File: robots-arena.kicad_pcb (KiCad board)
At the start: 2 copper layers, 86.4 x 54.6 mm, 48 parts, among them J1 SMA, P1 CONN_01X03, P10 CONN_01X03, P11 CONN_01X04, P12 CONN_01X05, P13 CONN_01X04, P2 CONN_01X03, P3 CONN_01X03, P4 CONN_01X03, P5 CONN_01X03, P6 CONN_01X03, P7 CONN_01X03, P8 CONN_23X2, P9 CONN_23X2, SW1 DIPS_02, U1 MPU-9150, U2 FGPMMOPA6H, U3 LPS331AP, U4 CAT24C256W

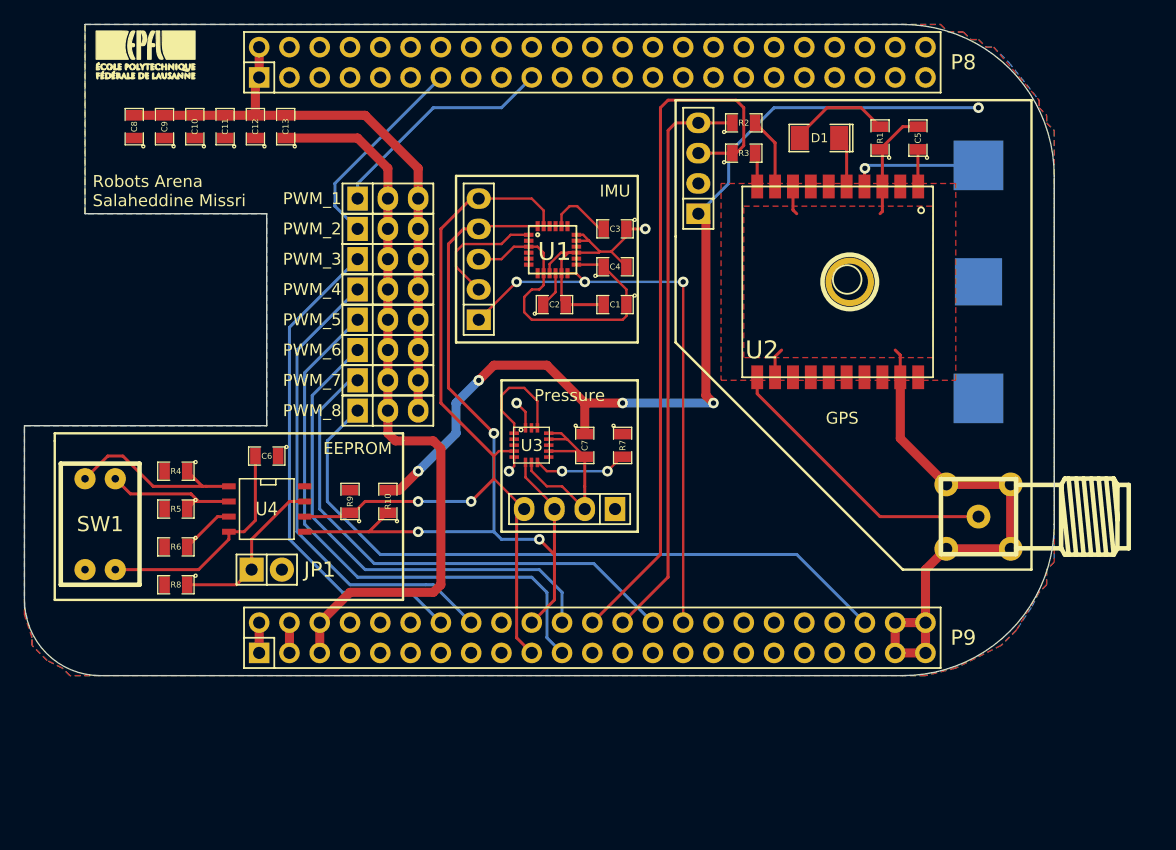
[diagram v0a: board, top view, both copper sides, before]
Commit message: .sch done, .net done, components on PCB done
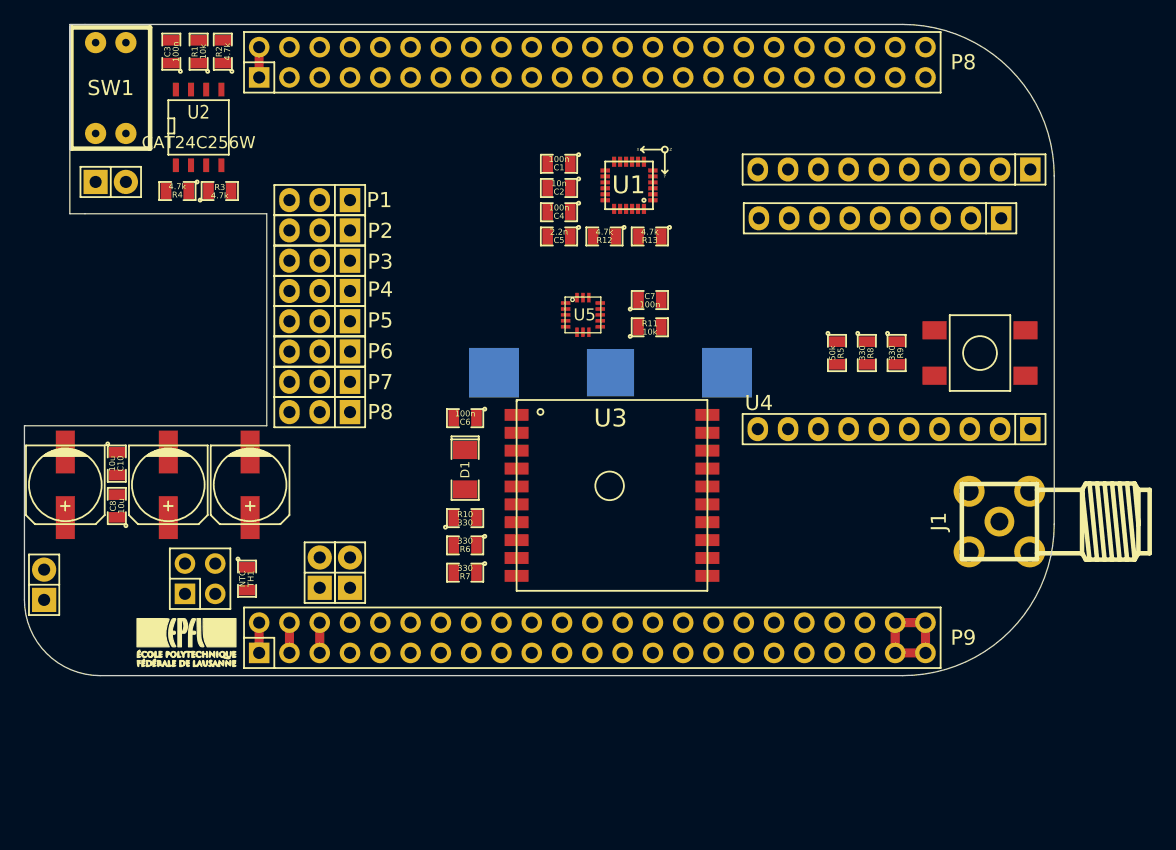
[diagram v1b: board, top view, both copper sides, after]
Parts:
- removed 1PIN: P***, Connect:1pin
- removed C13: 470u, SMD_Packages:SMD-0805
- removed the G*** at (172.7, 108.6)
- removed P10: CONN_01X03, Pin_Headers:Pin_Header_Straight_1x03
- added JP2: JUMPER, Pin_Headers:Pin_Header_Straight_1x02, F.Cu at (127.0, 113.3)
- added JP3: JUMPER, Pin_Headers:Pin_Header_Straight_1x02, F.Cu at (129.5, 113.3)
- added P8: CONN_PWM, Pin_Headers:Pin_Header_Straight_1x03, F.Cu at (127.0, 99.8)
- added R11: 10k, SMD_Packages:SMD-0805, F.Cu at (154.7, 92.7)
- added R12: 4.7k, SMD_Packages:SMD-0805, F.Cu at (150.9, 85.1)
- added R13: 4.7k, SMD_Packages:SMD-0805, F.Cu at (154.7, 85.1)
- added SW2: SW_PUSH, RA_connectors:SW_PUSH_SMD, F.Cu at (182.4, 94.2)
- added TH1: NTC, SMD_Packages:SMD-0805, F.Cu at (120.9, 113.8)
- added U5: LPS331AP, RA_sensors:LPS331AP, F.Cu at (147.6, 90.2)
- BT1: footprint RobotsArena:BK-885 -> RA_connectors:BK-885
- C1: value 10n -> 100n
- C11, C12, C9: value 10u -> 470u; footprint SMD_Packages:SMD-0805 -> Capacitors_SMD:c_elec_6.3x7.7
- C2: value 100n -> 10n
- C3: value 2.2n -> 100n
- C5: value 100n -> 2.2n
- J1: footprint RobotsArena:SMA -> RA_connectors:SMA-CONN
- P1, P2, P3, P4, P5, P6, P7: value CONN_01X03 -> CONN_PWM
- P11: value CONN_01X04 -> CONN_01X09; footprint Pin_Headers:Pin_Header_Straight_1x04 -> Pin_Headers:Pin_Header_Straight_1x09
- P12: value CONN_01X05 -> CONN_02X02; footprint Pin_Headers:Pin_Header_Straight_1x05 -> Pin_Headers:Pin_Header_Straight_2x02
- P13: value CONN_01X04 -> JST_2; footprint Pin_Headers:Pin_Header_Straight_1x04 -> Pin_Headers:Pin_Header_Straight_1x02
- R1: value 330 -> 10k
- R10, R6, R9: value 4.7k -> 330
- R2, R3: value 330 -> 4.7k
- R5: value 4.7k -> 50k
- R7, R8: value 10k -> 330
- SW1: value DIPS_02 -> DIPSW_02; footprint RobotsArena:DIPS-DS02 -> RA_connectors:DIPS-DS02
- U1: footprint RobotsArena:MPU-9150 -> RA_sensors:MPU-9150
- U2: value FGPMMOPA6H -> CAT24C256W; footprint RobotsArena:10011-FGPMMOPA6H -> SMD_Packages:SOIC-8-N
- U3: value LPS331AP -> MTK339; footprint RobotsArena:LPS331AP -> RA_sensors:FGPMMOPA6H
- U4: value CAT24C256W -> XBee_Header; footprint SMD_Packages:SOIC-8-N -> RA_connectors:XBEE-HEADER
- moved U2 61.8 mm to (116.8, 75.9), turned to 0 degrees
- moved R8 61.1 mm to (172.9, 94.9), turned to 270 degrees
- moved U4 57.9 mm to (177.8, 90.7)
- moved R1 57.6 mm to (116.8, 69.6)
- moved R5 57.0 mm to (170.4, 94.9), turned to 270 degrees
- moved G*** 49.4 mm to (115.8, 119.1)
- moved R9 47.5 mm to (175.4, 94.9), turned to 270 degrees
- moved P13 44.5 mm to (103.9, 114.3), turned to 90 degrees
- moved R2 44.1 mm to (118.9, 69.6), turned to 90 degrees
- moved R3 44.1 mm to (118.6, 81.3)
- moved D1 40.7 mm to (139.2, 104.6), turned to 270 degrees
- moved C3 40.1 mm to (114.6, 69.6), turned to 90 degrees
- moved SW1 36.6 mm to (109.5, 72.6)
- moved P12 35.6 mm to (117.0, 113.8), turned to 0 degrees
- moved JP1 35.0 mm to (109.5, 80.5)
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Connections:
- C10 pad 1: 3V3 -> +5V
- C11 pad 1: 3V3 -> +5V
- C12 pad 1: 3V3 -> +5V
- C2 pad 1: Net-(C2-Pad1) -> 3V3
- C3 pad 1: DGND -> 3V3
- C3 pad 2: Net-(C3-Pad2) -> DGND
- C4 pad 1: 3V3 -> Net-(C4-Pad1)
- C5 pad 1: 3V3 -> Net-(C5-Pad1)
- P11 pad 1: 3V3 -> Net-(P11-Pad1)
- P11 pad 2: DGND -> Net-(P11-Pad2)
- P11 pad 3: UART_1_TX -> Net-(P11-Pad3)
- P11 pad 4: UART_1_RX -> Net-(P11-Pad4)
- P12 pad 1: INT_M -> SENSE
- P12 pad 2: DGND -> SENSE
- P12 pad 3: 3V3 -> BAT-
- P12 pad 4: I2C_2_SDA -> TS
- P13 pad 1: 3V3 -> BAT-
- P13 pad 2: DGND -> SENSE
- P8 pad 16: Net-(P8-Pad16) -> INT_M
- P8 pad 18: Net-(P8-Pad18) -> BEE_DTR
- P8 pad 31: Net-(P8-Pad31) -> UART_5_CTS
- P8 pad 32: Net-(P8-Pad32) -> UART_5_RTS
- P8 pad 37: Net-(P8-Pad37) -> UART_5_TX
- P8 pad 38: Net-(P8-Pad38) -> UART_5_RX
- P9 pad 30: INT_M -> Net-(P9-Pad30)
- P9 pad 5: +5V -> BBB_VDD_5V
- P9 pad 6: +5V -> BBB_VDD_5V
- P9 pad 7: Net-(P9-Pad7) -> BBB_SYS_5V
- P9 pad 8: Net-(P9-Pad8) -> BBB_SYS_5V
- R1 pad 1: DGND -> Net-(JP1-Pad1)
- R1 pad 2: Net-(D1-Pad2) -> 3V3
- R10 pad 1: I2C_2_SDA -> Net-(D1-Pad2)
- R10 pad 2: 3V3 -> DGND
- R2 pad 1: UART_1_RX -> Net-(R2-Pad1)
- R2 pad 2: Net-(R2-Pad2) -> 3V3
- R3 pad 1: UART_1_TX -> Net-(R3-Pad1)
- R3 pad 2: Net-(R3-Pad2) -> 3V3
- R5 pad 1: Net-(R5-Pad1) -> 3V3
- R5 pad 2: 3V3 -> Net-(R5-Pad2)
- R6 pad 2: 3V3 -> UART_1_RX
- R7 pad 1: 3V3 -> Net-(R7-Pad1)
- R7 pad 2: Net-(R7-Pad2) -> UART_1_TX
- R8 pad 1: Net-(JP1-Pad1) -> Net-(R8-Pad1)
- R8 pad 2: 3V3 -> UART_5_RX
- R9 pad 1: I2C_2_SCL -> Net-(R9-Pad1)
- R9 pad 2: 3V3 -> UART_5_TX
- SW1 pad 1: DGND -> Net-(R4-Pad1)
- SW1 pad 2: DGND -> Net-(R3-Pad1)
- SW1 pad 3: Net-(R5-Pad1) -> DGND
- SW1 pad 4: Net-(R4-Pad1) -> DGND
- U1 pad 10: Net-(C2-Pad1) -> Net-(C4-Pad1)
- U1 pad 20: Net-(C3-Pad2) -> Net-(C5-Pad1)
- U2 pad 1: 3V3 -> Net-(R4-Pad1)
- U2 pad 2: Net-(U2-Pad2) -> Net-(R3-Pad1)
- U2 pad 3: DGND -> Net-(R2-Pad1)
- U2 pad 4: Net-(BT1-Pad1) -> DGND
- U2 pad 5: Net-(D1-Pad1) -> I2C_2_SDA
- U2 pad 6: Net-(U2-Pad6) -> I2C_2_SCL
- U2 pad 7: Net-(U2-Pad7) -> Net-(JP1-Pad1)
- U2 pad 8: DGND -> 3V3
- U3 pad 10: DGND -> Net-(R7-Pad1)
- U3 pad 11: Net-(U3-Pad11) -> Net-(J1-Pad1)
- U3 pad 13: DGND -> Net-(U3-Pad13)
- U3 pad 14: 3V3 -> Net-(U3-Pad14)
- U3 pad 15: 3V3 -> Net-(U3-Pad15)
- U3 pad 16: DGND -> Net-(U3-Pad16)
- U3 pad 3: Net-(U3-Pad3) -> DGND
- U3 pad 4: I2C_2_SCL -> Net-(BT1-Pad1)
- U3 pad 5: DGND -> Net-(D1-Pad1)
- U3 pad 6: I2C_2_SDA -> Net-(U3-Pad6)
- U3 pad 7: DGND -> Net-(U3-Pad7)
- U3 pad 8: Net-(R7-Pad2) -> DGND
- U3 pad 9: Net-(U3-Pad9) -> Net-(R6-Pad1)
- U4 pad 1: Net-(R4-Pad1) -> 3V3
- U4 pad 2: Net-(R5-Pad1) -> Net-(R8-Pad1)
- U4 pad 3: Net-(R6-Pad1) -> Net-(R9-Pad1)
- U4 pad 4: DGND -> Net-(P11-Pad1)
- U4 pad 5: I2C_2_SDA -> Net-(R5-Pad2)
- U4 pad 6: I2C_2_SCL -> Net-(U4-Pad6)
- U4 pad 7: Net-(JP1-Pad1) -> Net-(U4-Pad7)
- U4 pad 8: 3V3 -> Net-(U4-Pad8)
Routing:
- net DGND: track 193.1 -> 16.1 mm, vias 3 -> 0
- net 3V3: track 126.2 -> 2.54 mm, vias 5 -> 0
- net I2C_2_SDA: track 73.7 -> 0.00 mm, vias 3 -> 0
- net I2C_2_SCL: track 69.7 -> 0.00 mm, vias 2 -> 0
- net +5V: track 62.3 -> 0.00 mm
- net UART_1_TX: track 60.3 -> 0.00 mm
- net PWM_8: track 58.0 -> 0.00 mm
- net INT_M: track 48.8 -> 0.00 mm, vias 3 -> 0
- net UART_1_RX: track 49.1 -> 0.63 mm
- net PWM_5: track 47.3 -> 0.00 mm
- net PWM_7: track 44.4 -> 0.00 mm
- net PWM_6: track 42.3 -> 0.00 mm
- net PWM_3: track 41.5 -> 0.00 mm
- net PWM_4: track 40.2 -> 0.00 mm
- net Net-(J1-Pad1): track 24.2 -> 0.00 mm
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- removed copper zone on F.Cu, net 3V3
- removed copper zone on B.Cu, net DGND
- removed copper zone on F.Cu, net DGND
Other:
- outline, holes or cut-outs redrawn
- board text removed: "EEPROM"
- board text removed: "GPS"
- board text removed: "IMU"
- board text removed: "Laboratoire d'automatique Robots arena Salaheddine Missri"
- board text removed: "PWM_1"
- board text removed: "PWM_2"
- board text removed: "PWM_3"
- board text removed: "PWM_4"
- board text removed: "PWM_5"
- board text removed: "PWM_6"
- board text removed: "PWM_7"
- board text removed: "PWM_8"
- board text removed: "Pressure"
- board text removed: "Robots Arena Salaheddine Missri"

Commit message: layout in progress, corrected pwm order
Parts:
- moved R5 23.8 mm to (184.4, 75.7), turned to 90 degrees
- moved R8 21.3 mm to (182.1, 75.7), turned to 90 degrees
- moved R9 19.7 mm to (179.8, 75.7), turned to 90 degrees
- moved P11 12.2 mm to (176.5, 95.5)
- moved SW2 7.12 mm to (182.1, 87.1), turned to 180 degrees
- moved U5 1.44 mm to (148.6, 89.2)
- moved C7 0.80 mm to (154.9, 89.7)
- moved R11 0.80 mm to (154.9, 91.9)
- moved BT1 0.36 mm to (151.6, 96.8)
- moved C6 0.25 mm to (139.2, 100.1)
- moved P1 0.25 mm to (126.7, 82.0)
- moved P2 0.25 mm to (126.7, 84.6)
- moved P3 0.25 mm to (126.7, 87.1)
- moved P4 0.25 mm to (126.7, 89.7)
- moved P5 0.25 mm to (126.7, 92.2)
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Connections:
- net SENSE renamed BAT+
- P8 pad 13: PWM_2 -> PWM_1
- P8 pad 19: PWM_1 -> PWM_2
- P9 pad 14: PWM_3 -> PWM_8
- P9 pad 16: PWM_4 -> PWM_7
- P9 pad 21: PWM_5 -> PWM_6
- P9 pad 22: PWM_6 -> PWM_5
- P9 pad 28: PWM_7 -> PWM_4
- P9 pad 42: PWM_8 -> PWM_3
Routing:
- net PWM_3: track 0.00 -> 69.2 mm
- net PWM_4: track 0.00 -> 49.4 mm
- net UART_5_RTS: track 0.00 -> 43.8 mm
- net PWM_5: track 0.00 -> 39.7 mm
- net PWM_6: track 0.00 -> 39.5 mm
- net DGND: track 16.1 -> 52.9 mm
- net UART_5_CTS: track 0.00 -> 32.2 mm
- net PWM_7: track 0.00 -> 27.3 mm
- net PWM_2: track 0.00 -> 26.6 mm
- net Net-(J1-Pad1): track 0.00 -> 26.4 mm
- net Net-(R5-Pad2): track 0.00 -> 24.1 mm
- net Net-(P11-Pad1): track 0.00 -> 24.1 mm
- net PWM_8: track 0.00 -> 22.6 mm
- net Net-(P11-Pad6): track 0.00 -> 21.2 mm
- net +5V: track 0.00 -> 20.3 mm
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- added copper zone on F.Cu, net 3V3
- added copper zone on B.Cu, net DGND
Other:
- net class BigPower added: clearance 0.508, trace_width 0.508, via_dia 0.889, via_drill 0.508
- net class Default: clearance 0.254 -> 0.102; trace_width 0.254 -> 0.154; via_dia 0.889 -> 0.508; via_drill 0.635 -> 0.204
- net class Power added: clearance 0.254, trace_width 0.254, via_dia 0.889, via_drill 0.508
- rule trace_clearance: 0.254 -> 0.102
- rule trace_min: 0.2032 -> 0.154
- rule via_min_drill: 0.508 -> 0.154
- rule via_min_size: 0.889 -> 0.45

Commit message: Added adc connectors w/ 5 to 1.8V conversion
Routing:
- net BEE_DTR: track 0.00 -> 30.3 mm
- net INT_M: track 0.00 -> 17.8 mm, vias 0 -> 2
- net 3V3: track 19.6 -> 29.1 mm
- net DGND: track 52.9 -> 62.1 mm, vias 0 -> 1
- net UART_5_RTS: track 43.8 -> 45.0 mm
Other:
- net class BigPower: clearance 0.508 -> 0.154
- net class Default: clearance 0.102 -> 0.154
- net class Power: clearance 0.254 -> 0.154
- rule trace_clearance: 0.102 -> 0.154

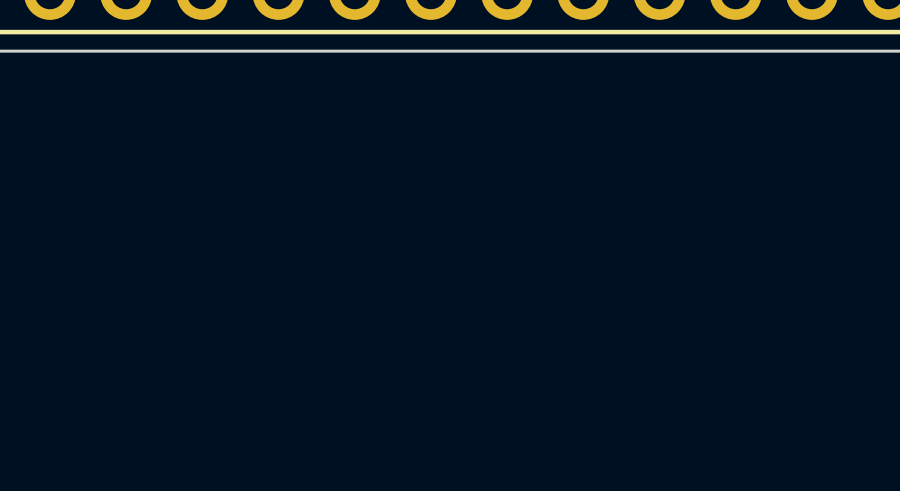
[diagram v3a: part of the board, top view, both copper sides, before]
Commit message: Update netlist & components footprints
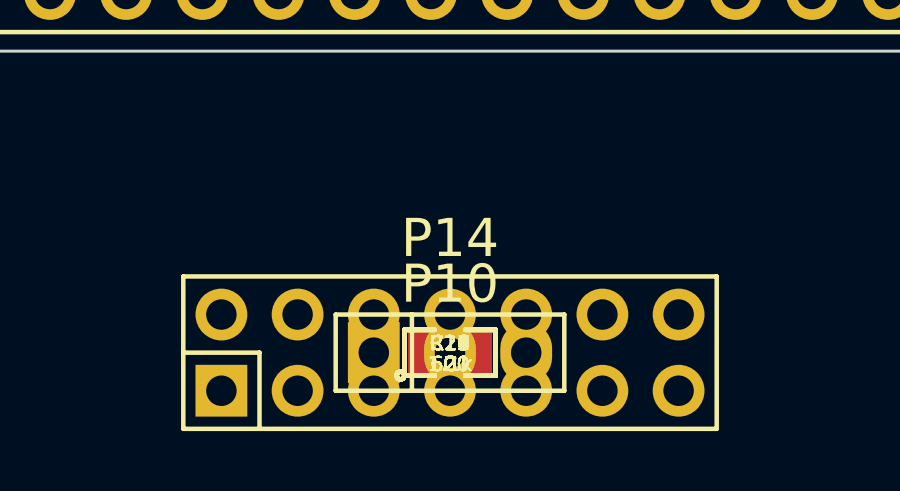
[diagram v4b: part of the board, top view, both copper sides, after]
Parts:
- added C13, C14, C15, C16, C17, C18, C19: C, SMD_Packages:SMD-0805, F.Cu at (145.4, 132.0)
- added P10: CONN_PWM, Pin_Headers:Pin_Header_Straight_1x03, F.Cu at (145.4, 132.0)
- added P14: CONN_02X07, Pin_Headers:Pin_Header_Straight_2x07, F.Cu at (145.4, 132.0)
- added R14, R16, R18, R20, R22, R24, R26: 1.1k, SMD_Packages:SMD-0805, F.Cu at (145.4, 132.0)
- added R15, R17, R19, R21, R23, R25, R27: 620, SMD_Packages:SMD-0805, F.Cu at (145.4, 132.0)
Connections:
- net Net-(P9-Pad32) renamed /BeagleBone Connections/VDD_ADC
- P9 pad 33: Net-(P9-Pad33) -> ADC_IN_6
- P9 pad 34: Net-(P9-Pad34) -> DGND
- P9 pad 35: Net-(P9-Pad35) -> ADC_IN_4
- P9 pad 36: Net-(P9-Pad36) -> ADC_IN_5
- P9 pad 37: Net-(P9-Pad37) -> ADC_IN_2
- P9 pad 38: Net-(P9-Pad38) -> ADC_IN_3
- P9 pad 39: Net-(P9-Pad39) -> ADC_IN_0
- P9 pad 40: Net-(P9-Pad40) -> ADC_IN_1

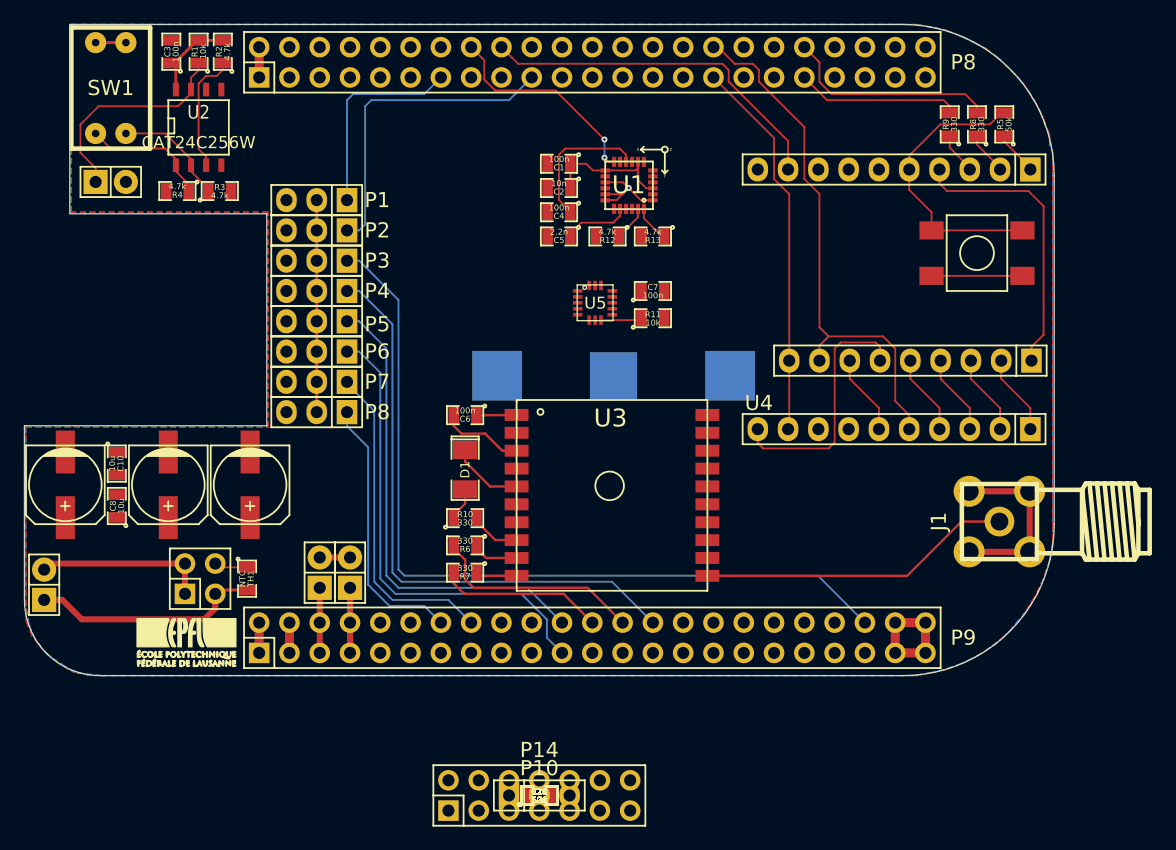
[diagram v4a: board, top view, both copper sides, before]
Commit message: Place components on PCB & ajust nets to stay w/ 2 layers
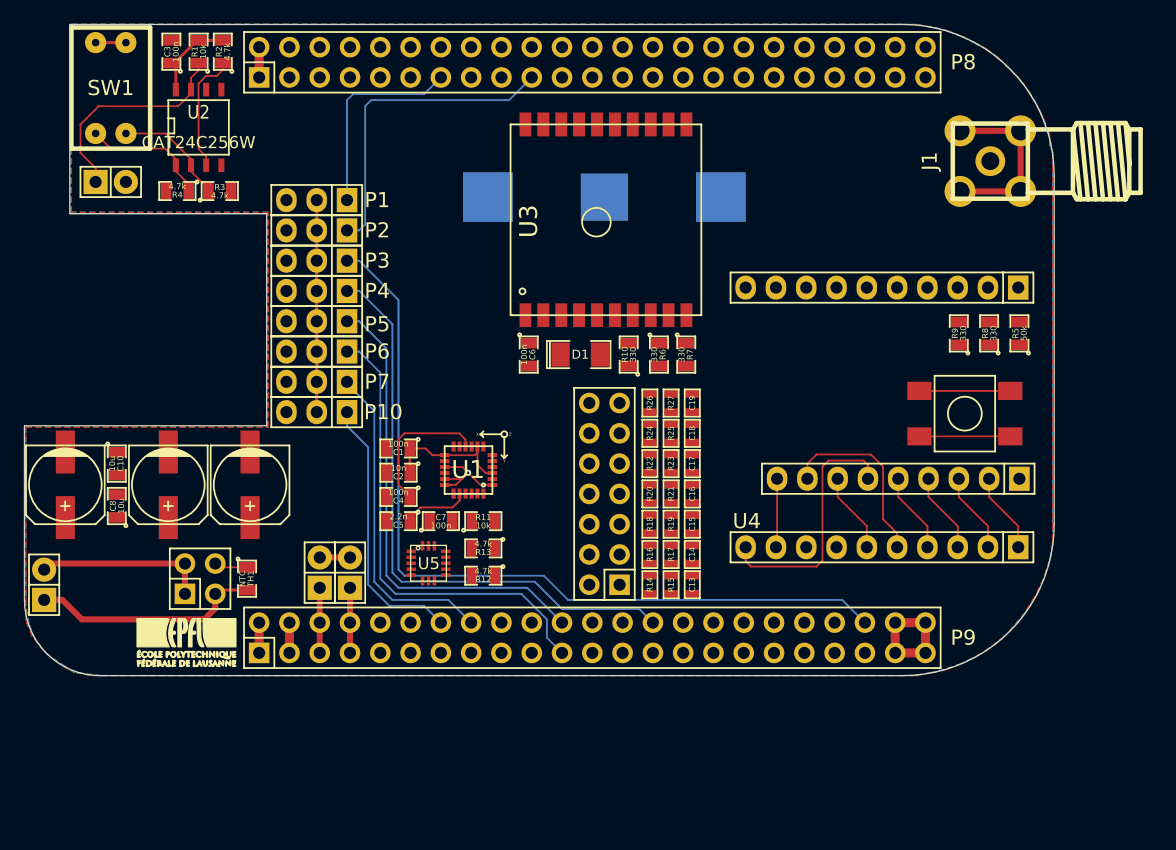
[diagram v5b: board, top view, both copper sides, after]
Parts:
- removed the P10 at (145.4, 132.0)
- C13, C14, C15, C16, C17, C18, C19, R14, R15, R16, R17, R18, R19, R20, R21, R22, R23, R24, R25, R26, R27: footprint SMD_Packages:SMD-0805 -> SMD_Packages:SMD-0603
- moved C19 35.3 mm to (158.2, 99.1), turned to 90 degrees
- moved R27 34.7 mm to (156.5, 99.1), turned to 90 degrees
- moved R26 34.2 mm to (154.7, 99.1), turned to 90 degrees
- moved C18 33.0 mm to (158.2, 101.6), turned to 90 degrees
- moved R25 32.3 mm to (156.5, 101.6), turned to 90 degrees
- moved R24 31.8 mm to (154.7, 101.6), turned to 90 degrees
- moved C17 30.6 mm to (158.2, 104.1), turned to 90 degrees
- moved R12 30.3 mm to (140.7, 113.5)
- moved J1 30.2 mm to (183.2, 78.8)
- moved R23 29.9 mm to (156.5, 104.1), turned to 90 degrees
- moved R13 29.8 mm to (140.7, 111.3)
- moved R22 29.3 mm to (154.7, 104.1), turned to 90 degrees
- moved C16 28.4 mm to (158.2, 106.7), turned to 90 degrees
- moved R21 27.6 mm to (156.5, 106.7), turned to 90 degrees
- moved C1 27.4 mm to (133.6, 102.9)
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- renumbered P8 to P10
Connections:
- C13 pad 1: ADC_IN_0 -> ADC_IN_6
- C14 pad 1: ADC_IN_1 -> ADC_IN_4
- C15 pad 1: ADC_IN_2 -> ADC_IN_5
- C16 pad 1: ADC_IN_3 -> ADC_IN_2
- C17 pad 1: ADC_IN_4 -> ADC_IN_3
- C18 pad 1: ADC_IN_5 -> ADC_IN_0
- C19 pad 1: ADC_IN_6 -> ADC_IN_1
- P14 pad 1: ADC_RAW_0 -> ADC_RAW_6
- P14 pad 11: ADC_RAW_5 -> ADC_RAW_0
- P14 pad 13: ADC_RAW_6 -> ADC_RAW_1
- P14 pad 3: ADC_RAW_1 -> ADC_RAW_4
- P14 pad 5: ADC_RAW_2 -> ADC_RAW_5
- P14 pad 7: ADC_RAW_3 -> ADC_RAW_2
- P14 pad 9: ADC_RAW_4 -> ADC_RAW_3
- R14 pad 1: ADC_RAW_0 -> ADC_RAW_6
- R14 pad 2: ADC_IN_0 -> ADC_IN_6
- R15 pad 1: ADC_IN_0 -> ADC_IN_6
- R16 pad 1: ADC_RAW_1 -> ADC_RAW_4
- R16 pad 2: ADC_IN_1 -> ADC_IN_4
- R17 pad 1: ADC_IN_1 -> ADC_IN_4
- R18 pad 1: ADC_RAW_2 -> ADC_RAW_5
- R18 pad 2: ADC_IN_2 -> ADC_IN_5
- R19 pad 1: ADC_IN_2 -> ADC_IN_5
- R20 pad 1: ADC_RAW_3 -> ADC_RAW_2
- R20 pad 2: ADC_IN_3 -> ADC_IN_2
- R21 pad 1: ADC_IN_3 -> ADC_IN_2
- R22 pad 1: ADC_RAW_4 -> ADC_RAW_3
- R22 pad 2: ADC_IN_4 -> ADC_IN_3
- R23 pad 1: ADC_IN_4 -> ADC_IN_3
- R24 pad 1: ADC_RAW_5 -> ADC_RAW_0
- R24 pad 2: ADC_IN_5 -> ADC_IN_0
- R25 pad 1: ADC_IN_5 -> ADC_IN_0
- R26 pad 1: ADC_RAW_6 -> ADC_RAW_1
- R26 pad 2: ADC_IN_6 -> ADC_IN_1
- R27 pad 1: ADC_IN_6 -> ADC_IN_1
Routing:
- net BEE_DTR: track 30.3 -> 0.00 mm
- net UART_5_RTS: track 45.0 -> 16.0 mm
- net UART_5_CTS: track 32.2 -> 5.78 mm
- net Net-(J1-Pad1): track 26.4 -> 0.00 mm
- net Net-(P11-Pad1): track 24.1 -> 0.00 mm
- net UART_5_RX: track 18.1 -> 0.00 mm
- net UART_1_RX: track 18.6 -> 0.63 mm
- net INT_M: track 17.8 -> 0.00 mm, vias 2 -> 0
- net Net-(R5-Pad2): track 24.1 -> 7.62 mm
- net UART_1_TX: track 13.9 -> 0.00 mm
- net UART_5_TX: track 13.8 -> 0.00 mm
- net DGND: track 62.1 -> 50.6 mm
- net Net-(D1-Pad1): track 7.41 -> 0.00 mm
- net 3V3: track 29.1 -> 22.2 mm
- net Net-(R6-Pad1): track 3.95 -> 0.00 mm
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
